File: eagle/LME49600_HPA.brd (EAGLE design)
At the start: 100 x 80 mm, 20 parts, among them IC1 OPA2134P

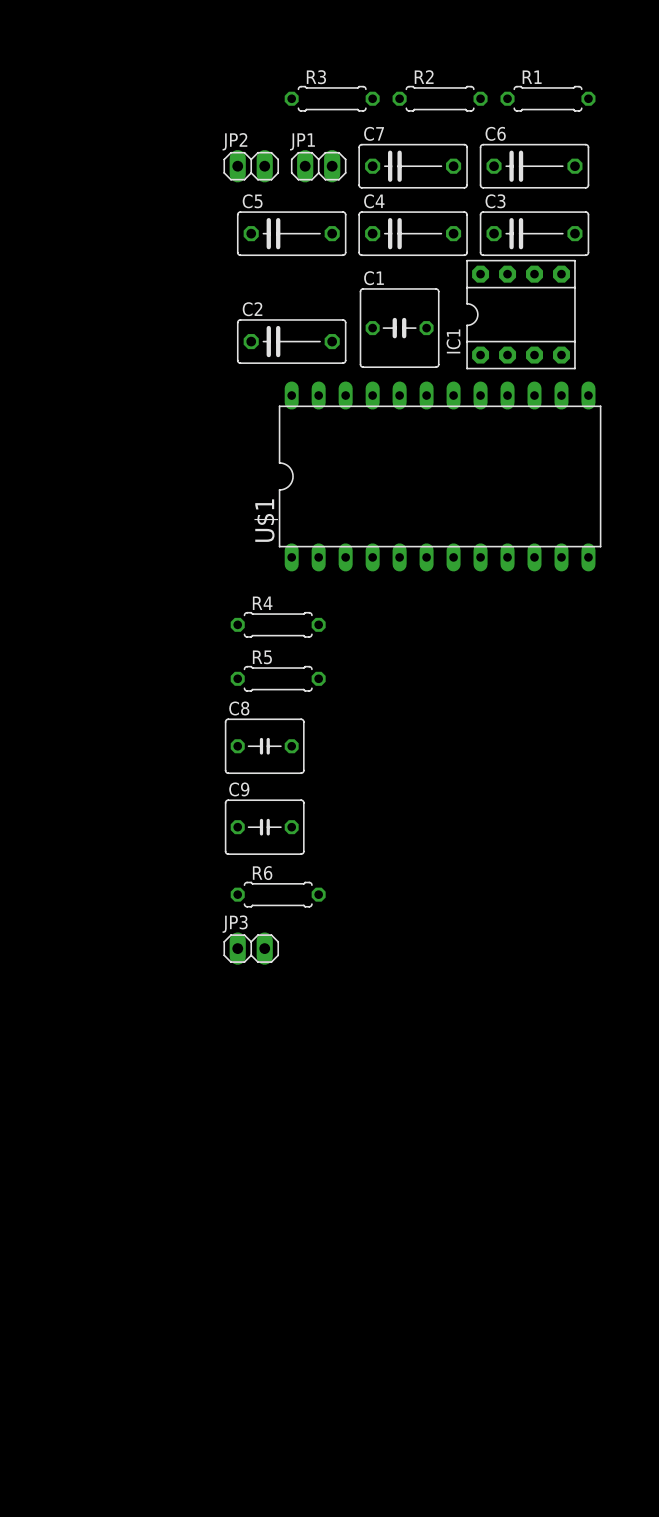
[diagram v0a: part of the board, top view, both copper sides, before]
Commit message: Add: Power Supply
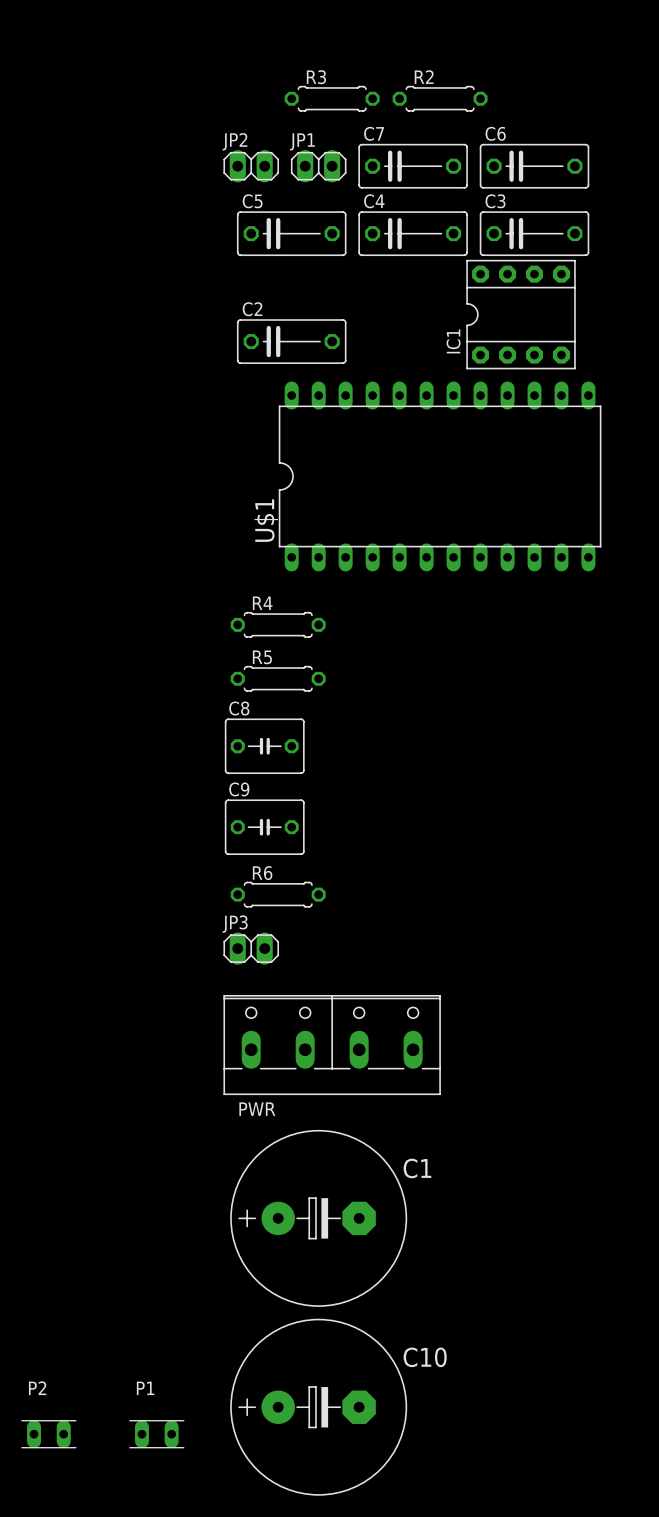
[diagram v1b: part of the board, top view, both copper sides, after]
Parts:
- removed R1: 47k, rcl:0207/7
- added C10: 470uF, rcl:E7,5-16
- added P1, P2: POLYSWITCH, mylib2:POLYSWITCH
- added PWR: (no value), con-wago-508:W237-4P
- C1: value 2.2uF -> 470uF; device rcl:C050-075X075 -> rcl:E7,5-16
- JP3: value (none) -> SERVO
- moved C1 84.2 mm to (-39.4, -59.7)
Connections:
- removed net N$2: C1.2, IC1.3, R1.2
- new net N$9: P2.2, PWR.4
- new net P1: P1.2, PWR.1
- net AGND: now also C1.-, C10.+, PWR.2, PWR.3; no longer R1.1
- net N$1: now also IC1.3; no longer C1.1
- net V+: now also C1.+, P1.1
- net V-: now also C10.-, P2.1
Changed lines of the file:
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@@
 </autorouter>
 <elements>
-<element name="C1" library="rcl" package="C050-075X075" value="2.2uF" x="-31.75" y="24.13"/>
 <element name="C2" library="rcl" package="C075-042X103" value="0.1uF" x="-41.91" y="22.86"/>
 <element name="C3" library="rcl" package="C075-042X103" value="0.1uF" x="-19.05" y="33.02"/>
@@
 <element name="JP1" library="pinhead" package="1X02" value="IN" x="-39.37" y="39.37"/>
 <element name="JP2" library="pinhead" package="1X02" value="OUT" x="-45.72" y="39.37"/>
-<element name="R1" library="rcl" package="0207/7" value="47k" x="-17.78" y="45.72"/>
 <element name="R2" library="rcl" package="0207/7" value="1.2k" x="-27.94" y="45.72"/>
 <element name="R3" library="rcl" package="0207/7" value="1.2k" x="-38.1" y="45.72"/>
@@
 <element name="C9" library="rcl" package="C050-050X075" value="1.0uF" x="-44.45" y="-22.86"/>
 <element name="R6" library="rcl" package="0207/7" value="1.2k" x="-43.18" y="-29.21"/>
-<element name="JP3" library="pinhead" package="1X02" value="" x="-45.72" y="-34.29"/>
+<element name="JP3" library="pinhead" package="1X02" value="SERVO" x="-45.72" y="-34.29"/>
+<element name="PWR" library="con-wago-508" package="W237-4P" value="" x="-38.1" y="-43.18">
+<attribute name="OC_NEWARK" value="unknown" x="-38.1" y="-43.18" size="1.778" layer="27" display="off"/>
+<attribute name="MPN" value="" x="-38.1" y="-43.18" size="1.778" layer="27" display="off"/>
+<attribute name="MF" value="" x="-38.1" y="-43.18" size="1.778" layer="27" display="off"/>
+<attribute name="OC_FARNELL" value="unknown" x="-38.1" y="-43.18" size="1.778" layer="27" display="off"/>
+</element>
+<element name="C1" library="rcl" package="E7,5-16" value="470uF" x="-39.37" y="-59.69"/>
+<element name="C10" library="rcl" package="E7,5-16" value="470uF" x="-39.37" y="-77.47"/>
+<element name="P1" library="mylib2" package="POLYSWITCH" value="POLYSWITCH" x="-54.61" y="-80.01"/>
+<element name="P2" library="mylib2" package="POLYSWITCH" value="POLYSWITCH" x="-64.77" y="-80.01"/>
 </elements>
 <signals>
-<signal name="N$1">
-<contactref element="JP1" pad="1"/>
-<contactref element="C1" pad="1"/>
-<wire x1="-40.64" y1="39.37" x2="-34.29" y2="24.13" width="0" layer="19" extent="1-1"/>
-</signal>
-<signal name="N$2">
-<contactref element="C1" pad="2"/>
-<contactref element="R1" pad="2"/>
-<contactref element="IC1" pad="3"/>
-<wire x1="-19.05" y1="21.59" x2="-13.97" y2="45.72" width="0" layer="19" extent="1-1"/>
-<wire x1="-29.21" y1="24.13" x2="-19.05" y2="21.59" width="0" layer="19" extent="1-1"/>
-</signal>
 <signal name="AGND">
 <contactref element="JP1" pad="2"/>
-<contactref element="R1" pad="1"/>
 <contactref element="R2" pad="1"/>
 <contactref element="C3" pad="2"/>
@@
 <contactref element="JP3" pad="2"/>
 <contactref element="JP2" pad="2"/>
+<contactref element="PWR" pad="3"/>
+<contactref element="C1" pad="-"/>
+<contactref element="PWR" pad="2"/>
+<contactref element="C10" pad="+"/>
+<wire x1="-35.56" y1="-59.69" x2="-43.18" y2="-77.47" width="0" layer="19" extent="1-1"/>
+<wire x1="-35.56" y1="-43.815" x2="-35.56" y2="-59.69" width="0" layer="19" extent="1-1"/>
+<wire x1="-40.64" y1="-43.815" x2="-35.56" y2="-43.815" width="0" layer="19" extent="1-1"/>
+<wire x1="-44.45" y1="-34.29" x2="-40.64" y2="-43.815" width="0" layer="19" extent="1-1"/>
 <wire x1="-41.91" y1="-22.86" x2="-44.45" y2="-34.29" width="0" layer="19" extent="1-1"/>
 <wire x1="-46.99" y1="-3.81" x2="-41.91" y2="-22.86" width="0" layer="19" extent="1-1"/>
@@
 <wire x1="-26.67" y1="39.37" x2="-31.75" y2="45.72" width="0" layer="19" extent="1-1"/>
 <wire x1="-26.67" y1="33.02" x2="-26.67" y2="39.37" width="0" layer="19" extent="1-1"/>
-<wire x1="-21.59" y1="45.72" x2="-26.67" y2="39.37" width="0" layer="19" extent="1-1"/>
-<wire x1="-15.24" y1="39.37" x2="-21.59" y2="45.72" width="0" layer="19" extent="1-1"/>
+<wire x1="-15.24" y1="39.37" x2="-26.67" y2="39.37" width="0" layer="19" extent="1-1"/>
 <wire x1="-15.24" y1="33.02" x2="-15.24" y2="39.37" width="0" layer="19" extent="1-1"/>
 </signal>
@@
 <contactref element="IC1" pad="4"/>
 <contactref element="C3" pad="1"/>
+<contactref element="C10" pad="-"/>
+<contactref element="P2" pad="1"/>
+<wire x1="-35.56" y1="-77.47" x2="-66.167" y2="-80.01" width="0" layer="19" extent="1-1"/>
+<wire x1="-39.37" y1="2.54" x2="-35.56" y2="-77.47" width="0" layer="19" extent="1-1"/>
 <wire x1="-29.21" y1="2.54" x2="-39.37" y2="2.54" width="0" layer="19" extent="1-1"/>
 <wire x1="-16.51" y1="21.59" x2="-29.21" y2="2.54" width="0" layer="19" extent="1-1"/>
@@
 <contactref element="IC1" pad="8"/>
 <contactref element="C2" pad="1"/>
-<wire x1="-34.29" y1="33.02" x2="-45.72" y2="22.86" width="0" layer="19" extent="1-1"/>
-<wire x1="-24.13" y1="29.21" x2="-34.29" y2="33.02" width="0" layer="19" extent="1-1"/>
+<contactref element="P1" pad="1"/>
+<contactref element="C1" pad="+"/>
+<wire x1="-43.18" y1="-59.69" x2="-56.007" y2="-80.01" width="0" layer="19" extent="1-1"/>
+<wire x1="-19.05" y1="2.54" x2="-43.18" y2="-59.69" width="0" layer="19" extent="1-1"/>
+<wire x1="-24.13" y1="29.21" x2="-19.05" y2="2.54" width="0" layer="19" extent="1-1"/>
 <wire x1="-22.86" y1="39.37" x2="-24.13" y2="29.21" width="0" layer="19" extent="1-1"/>
-<wire x1="-19.05" y1="2.54" x2="-24.13" y2="29.21" width="0" layer="19" extent="1-1"/>
+<wire x1="-34.29" y1="33.02" x2="-24.13" y2="29.21" width="0" layer="19" extent="1-1"/>
+<wire x1="-45.72" y1="22.86" x2="-34.29" y2="33.02" width="0" layer="19" extent="1-1"/>
 </signal>
 <signal name="N$6">
@@
 <wire x1="-34.29" y1="45.72" x2="-46.99" y2="39.37" width="0" layer="19" extent="1-1"/>
 </signal>
+<signal name="N$1">
+<contactref element="IC1" pad="3"/>
+<contactref element="JP1" pad="1"/>
+<wire x1="-40.64" y1="39.37" x2="-19.05" y2="21.59" width="0" layer="19" extent="1-1"/>
+</signal>
+<signal name="P1">
+<contactref element="P1" pad="2"/>
+<contactref element="PWR" pad="1"/>
+<wire x1="-45.72" y1="-43.815" x2="-53.213" y2="-80.01" width="0" layer="19" extent="1-1"/>
+</signal>
+<signal name="N$9">
+<contactref element="P2" pad="2"/>
+<contactref element="PWR" pad="4"/>
+<wire x1="-30.48" y1="-43.815" x2="-63.373" y2="-80.01" width="0" layer="19" extent="1-1"/>
+</signal>
 </signals>

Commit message: 2ch
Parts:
- added C11, C12, C13, C14: 0.1uF, rcl:C075-042X103
- added C15, C16: 4.7uF, rcl:C075-042X103
- added C17, C18: 1.0uF, rcl:C050-050X075
- added IC2: OPA2134P, burr-brown:DIL08
- added JP4: IN, pinhead:1X02
- added JP5: OUT, pinhead:1X02
- added JP6: SERVO, pinhead:1X02
- added R1, R10, R7: 1.2k, rcl:0207/7
- added R8, R9: 1M, rcl:0207/7
- added U$2: LME49600_BRD, mylib2:DIL24-6
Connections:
- new net N$10: C18.1, IC2.6, R9.2
- new net N$12: C17.2, IC2.7, JP6.1, R10.1
- new net N$13: JP5.1, R7.2, R9.1, U$2.8
- new net N$15: IC2.3, JP4.1
- new net N$2: IC2.2, R1.2, R10.2, R7.1
- new net N$4: IC2.1, U$2.4
- new net N$5: C17.1, IC2.5, R8.2
- net AGND: now also C11.2, C12.2, C13.2, C14.2, C15.2, C16.2, C18.2, JP4.2, JP5.2, JP6.2, R1.1, R8.1
- net V+: now also C11.1, C13.1, C15.1, IC2.8, U$2.10
- net V-: now also C12.1, C14.1, C16.1, IC2.4, U$2.2, U$2.6
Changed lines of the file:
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@@
 <element name="P1" library="mylib2" package="POLYSWITCH" value="POLYSWITCH" x="-54.61" y="-80.01"/>
 <element name="P2" library="mylib2" package="POLYSWITCH" value="POLYSWITCH" x="-64.77" y="-80.01"/>
+<element name="JP4" library="pinhead" package="1X02" value="IN" x="-64.77" y="-120.65"/>
+<element name="JP5" library="pinhead" package="1X02" value="OUT" x="-58.42" y="-120.65"/>
+<element name="IC2" library="burr-brown" package="DIL08" value="OPA2134P" x="-60.96" y="-111.76">
+<attribute name="OC_NEWARK" value="74K3897" x="-60.96" y="-106.68" size="1.778" layer="27" display="off"/>
+<attribute name="MPN" value="OPA2134PA" x="-60.96" y="-106.68" size="1.778" layer="27" display="off"/>
+<attribute name="MF" value="TEXAS INSTRUMENTS" x="-60.96" y="-106.68" size="1.778" layer="27" display="off"/>
+<attribute name="OC_FARNELL" value="1097574" x="-60.96" y="-106.68" size="1.778" layer="27" display="off"/>
+</element>
+<element name="R1" library="rcl" package="0207/7" value="1.2k" x="-52.07" y="-135.89"/>
+<element name="C11" library="rcl" package="C075-042X103" value="0.1uF" x="-49.53" y="-121.92"/>
+<element name="C12" library="rcl" package="C075-042X103" value="0.1uF" x="-38.1" y="-121.92"/>
+<element name="R7" library="rcl" package="0207/7" value="1.2k" x="-41.91" y="-135.89"/>
+<element name="U$2" library="mylib2" package="DIL24-6" value="LME49600_BRD" x="-50.8" y="-96.52"/>
+<element name="C13" library="rcl" package="C075-042X103" value="0.1uF" x="-62.23" y="-129.54"/>
+<element name="C14" library="rcl" package="C075-042X103" value="0.1uF" x="-50.8" y="-129.54"/>
+<element name="C15" library="rcl" package="C075-042X103" value="4.7uF" x="-39.37" y="-129.54"/>
+<element name="C16" library="rcl" package="C075-042X103" value="4.7uF" x="-62.23" y="-135.89"/>
+<element name="R8" library="rcl" package="0207/7" value="1M" x="-31.75" y="-135.89"/>
+<element name="R9" library="rcl" package="0207/7" value="1M" x="-63.5" y="-142.24"/>
+<element name="C17" library="rcl" package="C050-050X075" value="1.0uF" x="-49.53" y="-111.76"/>
+<element name="C18" library="rcl" package="C050-050X075" value="1.0uF" x="-40.64" y="-111.76"/>
+<element name="R10" library="rcl" package="0207/7" value="1.2k" x="-53.34" y="-142.24"/>
+<element name="JP6" library="pinhead" package="1X02" value="SERVO" x="-33.02" y="-110.49"/>
 </elements>
 <signals>
@@
 <contactref element="PWR" pad="2"/>
 <contactref element="C10" pad="+"/>
+<contactref element="JP4" pad="2"/>
+<contactref element="R1" pad="1"/>
+<contactref element="C12" pad="2"/>
+<contactref element="C11" pad="2"/>
+<contactref element="C15" pad="2"/>
+<contactref element="C13" pad="2"/>
+<contactref element="C14" pad="2"/>
+<contactref element="C16" pad="2"/>
+<contactref element="C18" pad="2"/>
+<contactref element="R8" pad="1"/>
+<contactref element="JP6" pad="2"/>
+<contactref element="JP5" pad="2"/>
+<wire x1="-55.88" y1="-135.89" x2="-58.42" y2="-135.89" width="0" layer="19" extent="1-1"/>
+<wire x1="-58.42" y1="-129.54" x2="-58.42" y2="-135.89" width="0" layer="19" extent="1-1"/>
+<wire x1="-57.15" y1="-120.65" x2="-58.42" y2="-129.54" width="0" layer="19" extent="1-1"/>
+<wire x1="-63.5" y1="-120.65" x2="-57.15" y2="-120.65" width="0" layer="19" extent="1-1"/>
+<wire x1="-46.99" y1="-129.54" x2="-55.88" y2="-135.89" width="0" layer="19" extent="1-1"/>
+<wire x1="-45.72" y1="-121.92" x2="-46.99" y2="-129.54" width="0" layer="19" extent="1-1"/>
+<wire x1="-35.56" y1="-129.54" x2="-46.99" y2="-129.54" width="0" layer="19" extent="1-1"/>
+<wire x1="-35.56" y1="-135.89" x2="-35.56" y2="-129.54" width="0" layer="19" extent="1-1"/>
+<wire x1="-34.29" y1="-121.92" x2="-35.56" y2="-129.54" width="0" layer="19" extent="1-1"/>
+<wire x1="-38.1" y1="-111.76" x2="-34.29" y2="-121.92" width="0" layer="19" extent="1-1"/>
+<wire x1="-31.75" y1="-110.49" x2="-38.1" y2="-111.76" width="0" layer="19" extent="1-1"/>
+<wire x1="-43.18" y1="-77.47" x2="-38.1" y2="-111.76" width="0" layer="19" extent="1-1"/>
 <wire x1="-35.56" y1="-59.69" x2="-43.18" y2="-77.47" width="0" layer="19" extent="1-1"/>
 <wire x1="-35.56" y1="-43.815" x2="-35.56" y2="-59.69" width="0" layer="19" extent="1-1"/>
@@
 <contactref element="C10" pad="-"/>
 <contactref element="P2" pad="1"/>
-<wire x1="-35.56" y1="-77.47" x2="-66.167" y2="-80.01" width="0" layer="19" extent="1-1"/>
+<contactref element="IC2" pad="4"/>
+<contactref element="U$2" pad="2"/>
+<contactref element="U$2" pad="6"/>
+<contactref element="C14" pad="1"/>
+<contactref element="C16" pad="1"/>
+<contactref element="C12" pad="1"/>
+<wire x1="-54.61" y1="-129.54" x2="-66.04" y2="-135.89" width="0" layer="19" extent="1-1"/>
+<wire x1="-57.15" y1="-115.57" x2="-54.61" y2="-129.54" width="0" layer="19" extent="1-1"/>
+<wire x1="-60.96" y1="-104.14" x2="-57.15" y2="-115.57" width="0" layer="19" extent="1-1"/>
+<wire x1="-50.8" y1="-104.14" x2="-60.96" y2="-104.14" width="0" layer="19" extent="1-1"/>
+<wire x1="-41.91" y1="-121.92" x2="-54.61" y2="-129.54" width="0" layer="19" extent="1-1"/>
+<wire x1="-66.167" y1="-80.01" x2="-60.96" y2="-104.14" width="0" layer="19" extent="1-1"/>
+<wire x1="-35.56" y1="-77.47" x2="-50.8" y2="-104.14" width="0" layer="19" extent="1-1"/>
 <wire x1="-39.37" y1="2.54" x2="-35.56" y2="-77.47" width="0" layer="19" extent="1-1"/>
 <wire x1="-29.21" y1="2.54" x2="-39.37" y2="2.54" width="0" layer="19" extent="1-1"/>
@@
 <contactref element="P1" pad="1"/>
 <contactref element="C1" pad="+"/>
+<contactref element="IC2" pad="8"/>
+<contactref element="U$2" pad="10"/>
+<contactref element="C15" pad="1"/>
+<contactref element="C13" pad="1"/>
+<contactref element="C11" pad="1"/>
+<wire x1="-53.34" y1="-121.92" x2="-66.04" y2="-129.54" width="0" layer="19" extent="1-1"/>
+<wire x1="-43.18" y1="-129.54" x2="-53.34" y2="-121.92" width="0" layer="19" extent="1-1"/>
+<wire x1="-64.77" y1="-107.95" x2="-53.34" y2="-121.92" width="0" layer="19" extent="1-1"/>
+<wire x1="-40.64" y1="-104.14" x2="-53.34" y2="-121.92" width="0" layer="19" extent="1-1"/>
+<wire x1="-56.007" y1="-80.01" x2="-40.64" y2="-104.14" width="0" layer="19" extent="1-1"/>
 <wire x1="-43.18" y1="-59.69" x2="-56.007" y2="-80.01" width="0" layer="19" extent="1-1"/>
 <wire x1="-19.05" y1="2.54" x2="-43.18" y2="-59.69" width="0" layer="19" extent="1-1"/>
@@
 <wire x1="-30.48" y1="-43.815" x2="-63.373" y2="-80.01" width="0" layer="19" extent="1-1"/>
 </signal>
+<signal name="N$2">
+<contactref element="R1" pad="2"/>
+<contactref element="IC2" pad="2"/>
+<contactref element="R7" pad="1"/>
+<contactref element="R10" pad="2"/>
+<wire x1="-48.26" y1="-135.89" x2="-49.53" y2="-142.24" width="0" layer="19" extent="1-1"/>
+<wire x1="-45.72" y1="-135.89" x2="-48.26" y2="-135.89" width="0" layer="19" extent="1-1"/>
+<wire x1="-62.23" y1="-115.57" x2="-48.26" y2="-135.89" width="0" layer="19" extent="1-1"/>
+</signal>
+<signal name="N$4">
+<contactref element="IC2" pad="1"/>
+<contactref element="U$2" pad="4"/>
+<wire x1="-55.88" y1="-104.14" x2="-64.77" y2="-115.57" width="0" layer="19" extent="1-1"/>
+</signal>
+<signal name="N$5">
+<contactref element="R8" pad="2"/>
+<contactref element="IC2" pad="5"/>
+<contactref element="C17" pad="1"/>
+<wire x1="-52.07" y1="-111.76" x2="-27.94" y2="-135.89" width="0" layer="19" extent="1-1"/>
+<wire x1="-57.15" y1="-107.95" x2="-52.07" y2="-111.76" width="0" layer="19" extent="1-1"/>
+</signal>
+<signal name="N$10">
+<contactref element="R9" pad="2"/>
+<contactref element="IC2" pad="6"/>
+<contactref element="C18" pad="1"/>
+<wire x1="-59.69" y1="-107.95" x2="-59.69" y2="-142.24" width="0" layer="19" extent="1-1"/>
+<wire x1="-43.18" y1="-111.76" x2="-59.69" y2="-107.95" width="0" layer="19" extent="1-1"/>
+</signal>
+<signal name="N$12">
+<contactref element="IC2" pad="7"/>
+<contactref element="C17" pad="2"/>
+<contactref element="R10" pad="1"/>
+<contactref element="JP6" pad="1"/>
+<wire x1="-46.99" y1="-111.76" x2="-57.15" y2="-142.24" width="0" layer="19" extent="1-1"/>
+<wire x1="-34.29" y1="-110.49" x2="-46.99" y2="-111.76" width="0" layer="19" extent="1-1"/>
+<wire x1="-62.23" y1="-107.95" x2="-46.99" y2="-111.76" width="0" layer="19" extent="1-1"/>
+</signal>
+<signal name="N$13">
+<contactref element="JP5" pad="1"/>
+<contactref element="U$2" pad="8"/>
+<contactref element="R7" pad="2"/>
+<contactref element="R9" pad="1"/>
+<wire x1="-59.69" y1="-120.65" x2="-67.31" y2="-142.24" width="0" layer="19" extent="1-1"/>
+<wire x1="-45.72" y1="-104.14" x2="-59.69" y2="-120.65" width="0" layer="19" extent="1-1"/>
+<wire x1="-38.1" y1="-135.89" x2="-59.69" y2="-120.65" width="0" layer="19" extent="1-1"/>
+</signal>
+<signal name="N$15">
+<contactref element="IC2" pad="3"/>
+<contactref element="JP4" pad="1"/>
+<wire x1="-59.69" y1="-115.57" x2="-66.04" y2="-120.65" width="0" layer="19" extent="1-1"/>
+</signal>
 </signals>

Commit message: bug fix
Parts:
- C15, C16: value 4.7uF -> 1.0uF; device rcl:C075-042X103 -> rcl:C050-050X075
- C17, C18: value 1.0uF -> 4.7uF; device rcl:C050-050X075 -> rcl:E2-4
- C6, C7: device rcl:C075-042X103 -> rcl:E2-4
- moved C7 138.0 mm to (-66.0, -94.0)
- moved C6 136.6 mm to (-66.0, -88.9)
- moved C18 41.7 mm to (-66.0, -144.8)
- moved C17 26.2 mm to (-43.2, -137.2)
- moved C16 25.7 mm to (-40.6, -121.9)
- moved C15 12.7 mm to (-49.5, -121.9)
- moved R1 10.2 mm to (-53.3, -146.1)
- moved R7 10.2 mm to (-43.2, -146.1)
- moved R8 10.2 mm to (-33.0, -146.1)
- moved C11 10.2 mm to (-49.5, -132.1)
- moved C12 10.2 mm to (-38.1, -132.1)
- moved JP6 10.2 mm to (-33.0, -120.7)
- moved U$2 10.2 mm to (-50.8, -106.7)
- moved C13 10.2 mm to (-62.2, -139.7)
- moved C14 10.2 mm to (-50.8, -139.7)
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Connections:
- net N$9 renamed PW-
- net P1 renamed PW+
- removed net N$12 (its old number): C17.2, IC2.7, JP6.1, R10.1
- new net N$9: C16.1, IC2.5, R9.2
- net AGND: now also C17.-, C18.+, C6.-, C7.+; no longer C15.2, C18.2, C6.2, C7.2
- net N$10: now also C15.2, IC2.7, JP6.1, R10.1; no longer C18.1, IC2.6, R9.2
- net N$5: now also C15.1, IC2.6; no longer C17.1, IC2.5
- net N$6: now also IC1.6; no longer IC1.5
- net N$8: now also IC1.5; no longer IC1.6
- net V+: now also C17.+, C6.+; no longer C15.1, C6.1
- net V-: now also C18.-, C7.-; no longer C16.1, C7.1
